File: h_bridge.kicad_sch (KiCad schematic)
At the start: 0 parts

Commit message: Added H-Bridge PCB Edits
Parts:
- added C27: 100pF, PCM_JLCPCB:C_0402, symbol PCM_JLCPCB-Capacitors:0402,100pF
- added C72, C73, C74, C75, C76, C77, C78, C79: 22uF, PCM_JLCPCB:C_0805, symbol PCM_JLCPCB-Capacitors:0805,22uF
- added C80: 100nF, PCM_JLCPCB:C_0805, symbol PCM_JLCPCB-Capacitors:0805,100nF
- added J17: MOT, TerminalBlock_Phoenix:TerminalBlock_Phoenix_MKDS-1,5-2-5.08_1x02_P5.08mm_Horizontal, symbol Connector_Generic:Conn_01x02
- added J18: Screw_Terminal_01x02, TerminalBlock_Phoenix:TerminalBlock_Phoenix_MKDS-1,5-2-5.08_1x02_P5.08mm_Horizontal, symbol Connector_Generic:Conn_01x02
- added JP4: ~, Jumper:SolderJumper-2_P1.3mm_Open_RoundedPad1.0x1.5mm, symbol Jumper:Jumper_2_Open
- added U10: TC118S, Package_SO:SOP-8_3.76x4.96mm_P1.27mm, symbol TC118S_H-Bridge:TC118S
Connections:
- new net: C27.1, J17.1 (Pin_1), U10.8 (OUTA)
- new net: C27.2, J17.2 (Pin_2), U10.5 (OUTB)
- new net +4.7V: JP4.1 (A)
- new net 5V: C72.1, C73.1, C74.1, C75.1, C76.1, C77.1, C78.1, C79.1, C80.1, J18.1 (Pin_1), JP4.2 (B), U10.4 (VDD)
- new net GND: C72.2, C73.2, C74.2, C75.2, C76.2, C77.2, C78.2, C79.2, C80.2, J18.2 (Pin_2), U10.6 (AGND), U10.7 (PGND)
- new net INA: U10.2 (INA)
- new net INB: U10.3 (INB)

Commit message: Getting JLCPCB Price
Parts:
- J17, J18: LCSC (none) -> C8465
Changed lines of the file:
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@@
 			)
 		)
-		(property "LCSC" ""
+		(property "LCSC" "C8465"
 			(at 180.34 78.74 0)
 			(effects
@@
 			)
 		)
-		(property "LCSC" ""
+		(property "LCSC" "C8465"
 			(at 180.34 34.29 0)
 			(effects

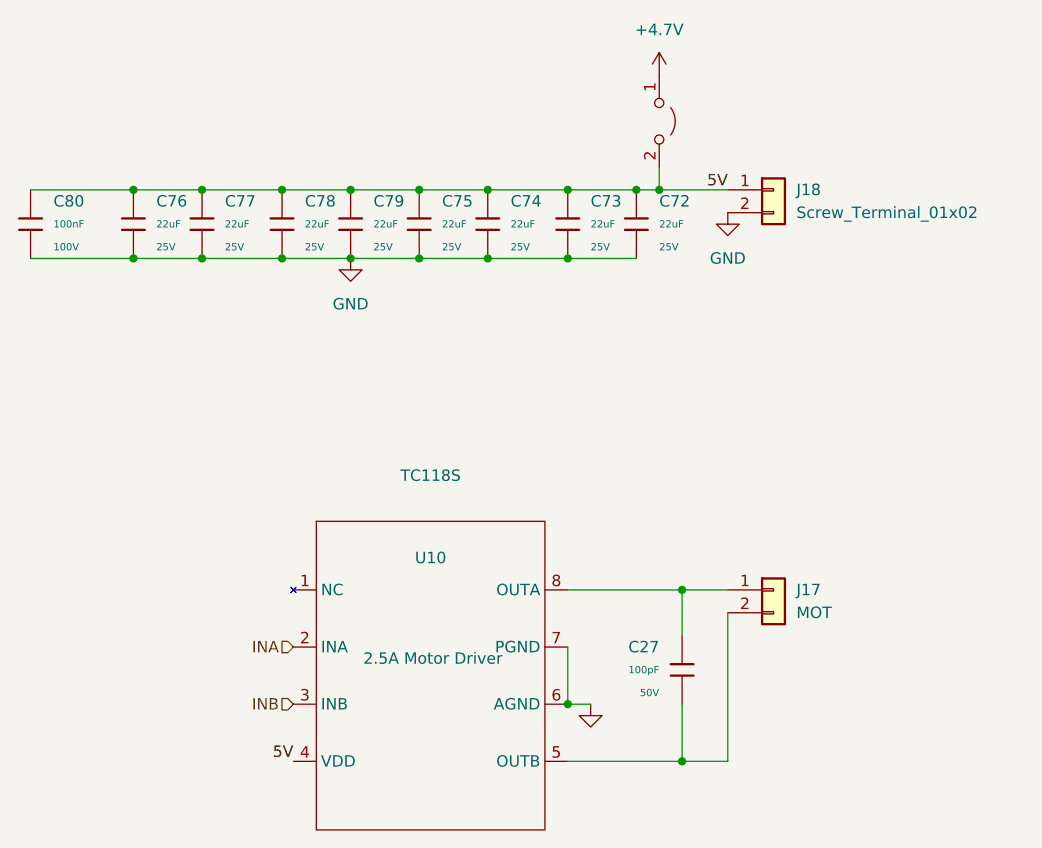
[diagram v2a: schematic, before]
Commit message: Replaced Jaron's LEDs
They were only for Standard Boards.
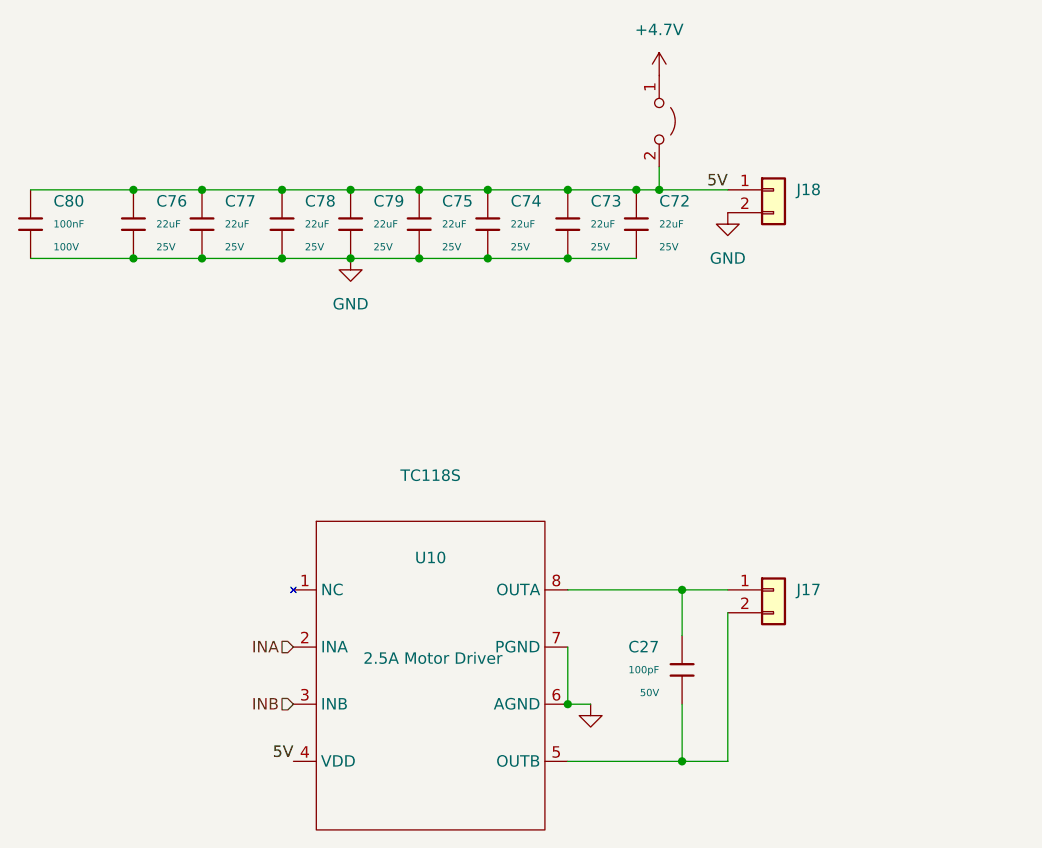
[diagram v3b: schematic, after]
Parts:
- J17: value MOT -> Screw_Terminal_01x02
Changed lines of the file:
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@@
 			)
 		)
-		(property "Value" "MOT"
+		(property "Value" "Screw_Terminal_01x02"
 			(at 182.88 81.2799 0)
 			(effects
@@
 				)
 				(justify left)
+				(hide yes)
 			)
 		)
@@
 				)
 				(justify left)
-			)
-		)
+				(hide yes)
+			)
+		)

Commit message: Initial v0.2
Fixed SCL-SDA swap, 3V3 on encoder, and 3D models for Kicad 10
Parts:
- JP4: value ~ -> (none)

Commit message: Placed the second ADC
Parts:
- C27: Manufacturer FH(Guangdong Fenghua Advanced Tech) -> (none)
- C72, C73, C74, C75, C76, C77, C78, C79, C80: Manufacturer Samsung Electro-Mechanics -> (none)
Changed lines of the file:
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@@
-			)
-		)
-		(property "Manufacturer" "Samsung Electro-Mechanics"
-			(at 140.97 38.1 0)
-			(hide yes)
-			(show_name no)
-			(do_not_autoplace no)
-			(effects
-				(font
-					(size 1.27 1.27)
-				)
 			)
 		)
@@
 			)
 		)
-		(property "Manufacturer" "Samsung Electro-Mechanics"
-			(at 148.59 38.1 0)
-			(hide yes)
-			(show_name no)
-			(do_not_autoplace no)
-			(effects
-				(font
-					(size 1.27 1.27)
-				)
-			)
-		)
 		(property "Part" "CL21A226MAQNNNE"
 			(at 148.59 38.1 0)
@@
 			)
 		)
-		(property "Manufacturer" "Samsung Electro-Mechanics"
-			(at 157.48 38.1 0)
-			(hide yes)
-			(show_name no)
-			(do_not_autoplace no)
-			(effects
-				(font
-					(size 1.27 1.27)
-				)
-			)
-		)
 		(property "Part" "CL21A226MAQNNNE"
 			(at 157.48 38.1 0)
@@
 			)
 		)
-		(property "Manufacturer" "Samsung Electro-Mechanics"
-			(at 165.1 38.1 0)
-			(hide yes)
-			(show_name no)
-			(do_not_autoplace no)
-			(effects
-				(font
-					(size 1.27 1.27)
-				)
-			)
-		)
 		(property "Part" "CL21A226MAQNNNE"
 			(at 165.1 38.1 0)
@@
 			)
 		)
-		(property "Manufacturer" "Samsung Electro-Mechanics"
-			(at 116.84 38.1 0)
-			(hide yes)
-			(show_name no)
-			(do_not_autoplace no)
-			(effects
-				(font
-					(size 1.27 1.27)
-				)
-			)
-		)
 		(property "Part" "CL21A226MAQNNNE"
 			(at 116.84 38.1 0)
@@
 			)
 		)
-		(property "Manufacturer" "Samsung Electro-Mechanics"
-			(at 133.35 38.1 0)
-			(hide yes)
-			(show_name no)
-			(do_not_autoplace no)
-			(effects
-				(font
-					(size 1.27 1.27)
-				)
-			)
-		)
 		(property "Part" "CL21A226MAQNNNE"
 			(at 133.35 38.1 0)
@@
 			)
 		)
-		(property "Manufacturer" "Samsung Electro-Mechanics"
-			(at 125.73 38.1 0)
-			(hide yes)
-			(show_name no)
-			(do_not_autoplace no)
-			(effects
-				(font
-					(size 1.27 1.27)
-				)
-			)
-		)
 		(property "Part" "CL21A226MAQNNNE"
 			(at 125.73 38.1 0)
@@
 			)
 		)
-		(property "Manufacturer" "Samsung Electro-Mechanics"
-			(at 97.79 38.1 0)
-			(hide yes)
-			(show_name no)
-			(do_not_autoplace no)
-			(effects
-				(font
-					(size 1.27 1.27)
-				)
-			)
-		)
 		(property "Part" "CL21B104KCFNNNE"
 			(at 97.79 38.1 0)
@@
 			)
 		)
-		(property "Manufacturer" "FH(Guangdong Fenghua Advanced Tech)"
-			(at 170.18 87.63 0)
-			(hide yes)
-			(show_name no)
-			(do_not_autoplace no)
-			(effects
-				(font
-					(size 1.27 1.27)
-				)
-			)
-		)
 		(property "Part" "0402CG101J500NT"
 			(at 170.18 87.63 0)
@@
 			(at 109.22 38.1 0)
 			(hide yes)
-			(show_name no)
-			(do_not_autoplace no)
-			(effects
-				(font
-					(size 1.27 1.27)
-				)
-			)
-		)
-		(property "Manufacturer" "Samsung Electro-Mechanics"
-			(at 109.22 38.1 0)
-			(hide yes)

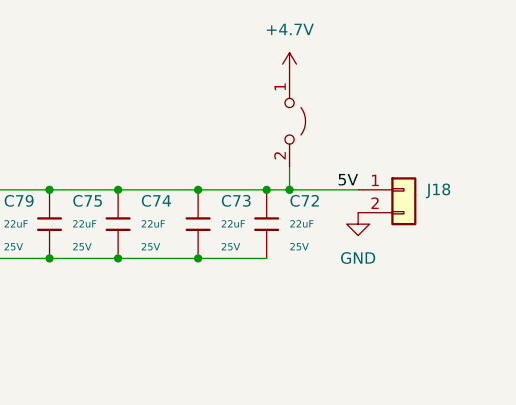
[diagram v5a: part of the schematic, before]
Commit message: Fixed sub-schematic versions
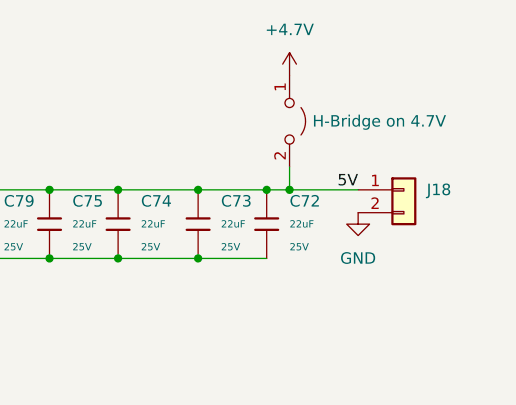
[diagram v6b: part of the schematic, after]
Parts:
- JP4: value (none) -> H-Bridge on 4.7V
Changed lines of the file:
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@@
 			)
 		)
-		(property "Value" ""
+		(property "Value" "H-Bridge on 4.7V"
 			(at 170.18 26.6699 90)
 			(show_name no)

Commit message: Label Tweaks
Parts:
- J17: value Screw_Terminal_01x02 -> H-OUT
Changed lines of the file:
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@@
 			)
 		)
-		(property "Value" "Screw_Terminal_01x02"
+		(property "Value" "H-OUT"
 			(at 182.88 81.2799 0)
 			(hide yes)

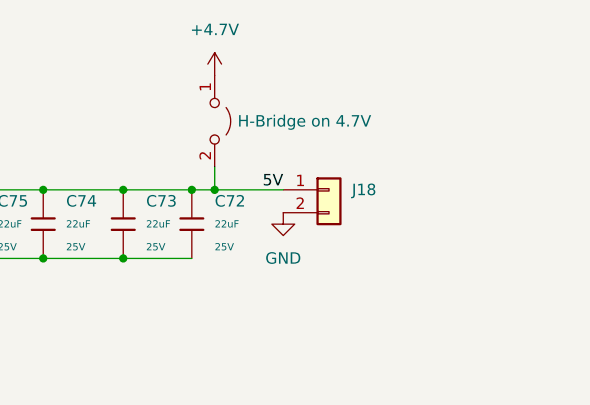
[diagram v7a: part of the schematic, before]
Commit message: H-IN on 4.7 V
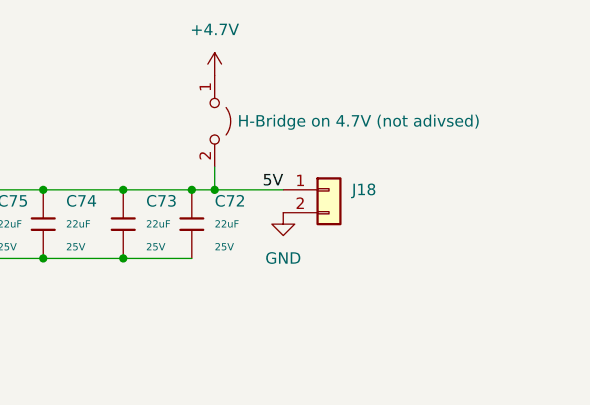
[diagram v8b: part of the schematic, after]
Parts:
- JP4: value H-Bridge on 4.7V -> H-Bridge on 4.7V (not adivsed)
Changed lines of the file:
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@@
 			)
 		)
-		(property "Value" "H-Bridge on 4.7V"
+		(property "Value" "H-Bridge on 4.7V (not adivsed)"
 			(at 170.18 26.6699 90)
 			(show_name no)
